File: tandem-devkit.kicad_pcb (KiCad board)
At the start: 2 copper layers, 95.4 x 100 mm, 88 parts, among them J101 Conn_01x02, J102 QWIIC I2C Connector, J301 ConnectorLCDFrontLight, J302 FPC24(0.5MM), J303 FPC10(0.5MM), Q301 2N7002, Q302 2N7002, Q303 AO3401A, U201 AMS1117-ADJ_SOT223

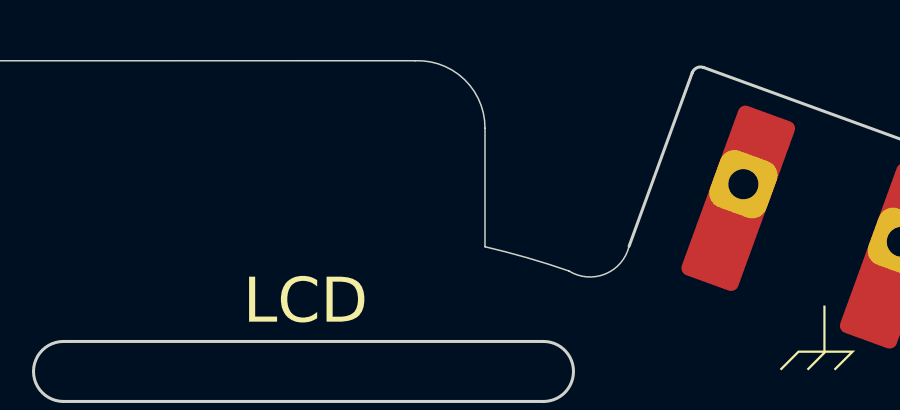
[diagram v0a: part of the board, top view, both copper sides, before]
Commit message: PCB: import JLCPCB 4-Layer board settings
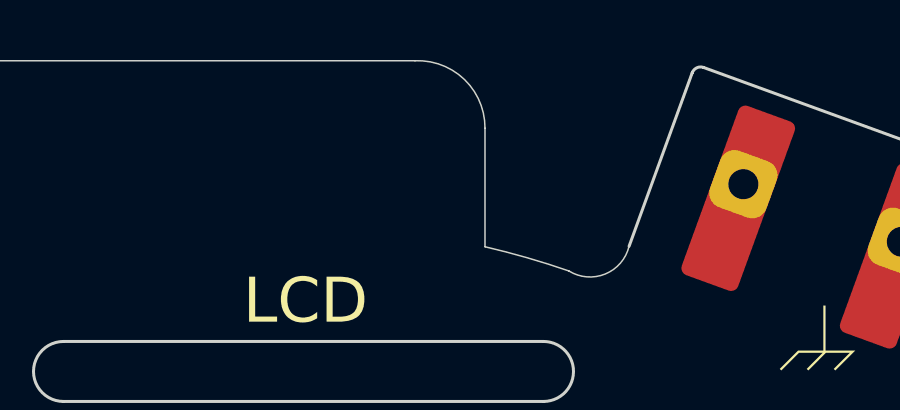
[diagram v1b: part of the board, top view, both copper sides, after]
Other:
- copper layers 2 -> 4
- rule pad_to_mask_clearance: 0.05 -> 0
- rule solder_mask_min_width: 0.2 -> 0.02
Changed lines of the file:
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@@
 (kicad_pcb (version 20211014) (generator pcbnew)
   (general
-    (thickness 1.6)
+    (thickness 4.69)
   )
   (paper "A4")
   (layers
     (0 "F.Cu" signal)
+    (1 "In1.Cu" power)
+    (2 "In2.Cu" power)
     (31 "B.Cu" signal)
-    (32 "B.Adhes" user "B.Adhesive")
-    (33 "F.Adhes" user "F.Adhesive")
     (34 "B.Paste" user)
     (35 "F.Paste" user)
@@
     (38 "B.Mask" user)
     (39 "F.Mask" user)
-    (40 "Dwgs.User" user "User.Drawings")
-    (41 "Cmts.User" user "User.Comments")
-    (42 "Eco1.User" user "User.Eco1")
-    (43 "Eco2.User" user "User.Eco2")
     (44 "Edge.Cuts" user)
     (45 "Margin" user)
@@
     (48 "B.Fab" user)
     (49 "F.Fab" user)
-    (50 "User.1" user "Housing_Outline")
-    (51 "User.2" user)
-    (52 "User.3" user)
-    (53 "User.4" user)
-    (54 "User.5" user)
-    (55 "User.6" user)
-    (56 "User.7" user)
-    (57 "User.8" user)
-    (58 "User.9" user)
   )
   (setup
@@
       (layer "F.Cu" (type "copper") (thickness 0.035))
       (layer "dielectric 1" (type "core") (thickness 1.51) (material "FR4") (epsilon_r 4.5) (loss_tangent 0.02))
+      (layer "In1.Cu" (type "copper") (thickness 0.035))
+      (layer "dielectric 2" (type "prepreg") (thickness 1.51) (material "FR4") (epsilon_r 4.5) (loss_tangent 0.02))
+      (layer "In2.Cu" (type "copper") (thickness 0.035))
+      (layer "dielectric 3" (type "core") (thickness 1.51) (material "FR4") (epsilon_r 4.5) (loss_tangent 0.02))
       (layer "B.Cu" (type "copper") (thickness 0.035))
-      (layer "B.Mask" (type "Bottom Solder Mask") (thickness 0.01))
+      (layer "B.Mask" (type "Bottom Solder Mask") (color "Red") (thickness 0.01))
       (layer "B.Paste" (type "Bottom Solder Paste"))
       (layer "B.SilkS" (type "Bottom Silk Screen"))
@@
       (dielectric_constraints yes)
     )
-    (pad_to_mask_clearance 0.05)
-    (solder_mask_min_width 0.2)
+    (pad_to_mask_clearance 0)
+    (solder_mask_min_width 0.02)
     (aux_axis_origin 284.994474 12.014472)
     (pcbplotparams
@@
     (fp_arc (start -45.696302 -20.932495) (mid -45.683648 -19.701061) (end -46.40509 -18.703007) (layer "Edge.Cuts") (width 0.05))
     (fp_arc (start 36.906133 -30.598692) (mid 37.06124 -30.768019) (end 37.290647 -30.777994) (layer "Edge.Cuts") (width 0.1))
-    (fp_arc (start 46.190086 -18.7) (mid 47.148177 -17.498337) (end 47.490086 -16) (layer "Edge.Cuts") (width 0.1))
+    (fp_arc (start 46.190086 -18.7) (mid 47.148169 -17.498338) (end 47.490086 -16) (layer "Edge.Cuts") (width 0.1))
     (fp_arc (start 47.490086 66.5) (mid 46.848778 68.178963) (end 45.25 69) (layer "Edge.Cuts") (width 0.05))
     (fp_arc (start -37.542423 -30.767616) (mid -37.30035 -30.764463) (end -37.121137 -30.601698) (layer "Edge.Cuts") (width 0.05))
-    (fp_arc (start 27.666822 -31.00341) (mid 29.316689 -30.377074) (end 30 -28.75) (layer "Edge.Cuts") (width 0.05))
+    (fp_arc (start 27.666822 -31.00341) (mid 29.316654 -30.377068) (end 30 -28.75) (layer "Edge.Cuts") (width 0.05))
     (fp_arc (start 30 -24.803362) (mid 31.407999 -24.436724) (end 32.79491 -23.996993) (layer "Edge.Cuts") (width 0.05))
     (pad "1" thru_hole roundrect locked (at -38.828584 -26.894123 20) (size 2 2) (drill 1) (layers *.Cu *.Mask) (roundrect_rratio 0.25))

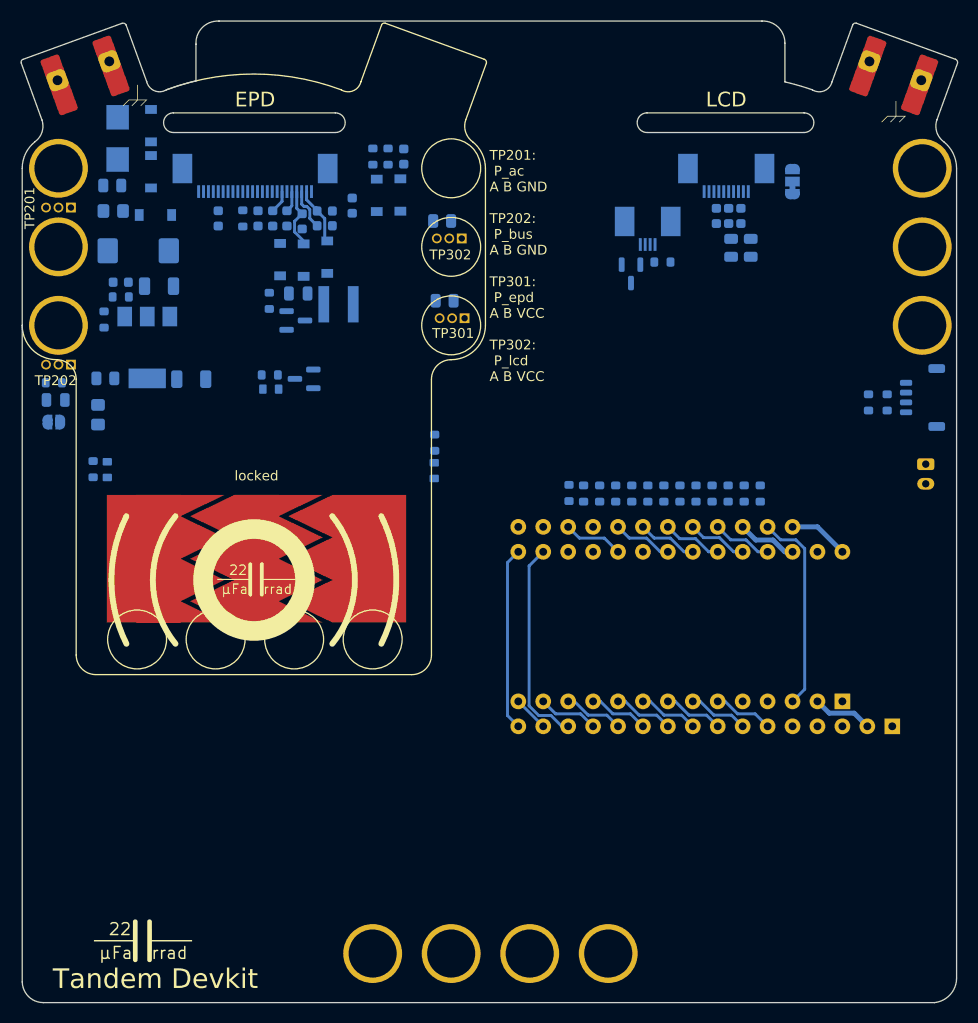
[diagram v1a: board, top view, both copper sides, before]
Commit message: PCB: fix DRC
- reduced track clearance for power and default net to fit between
  the pads of connectors
- rearranged epaper driver to adhere to DRC rules
- connected Feather and ItsyBitsy footprint and the related resistors
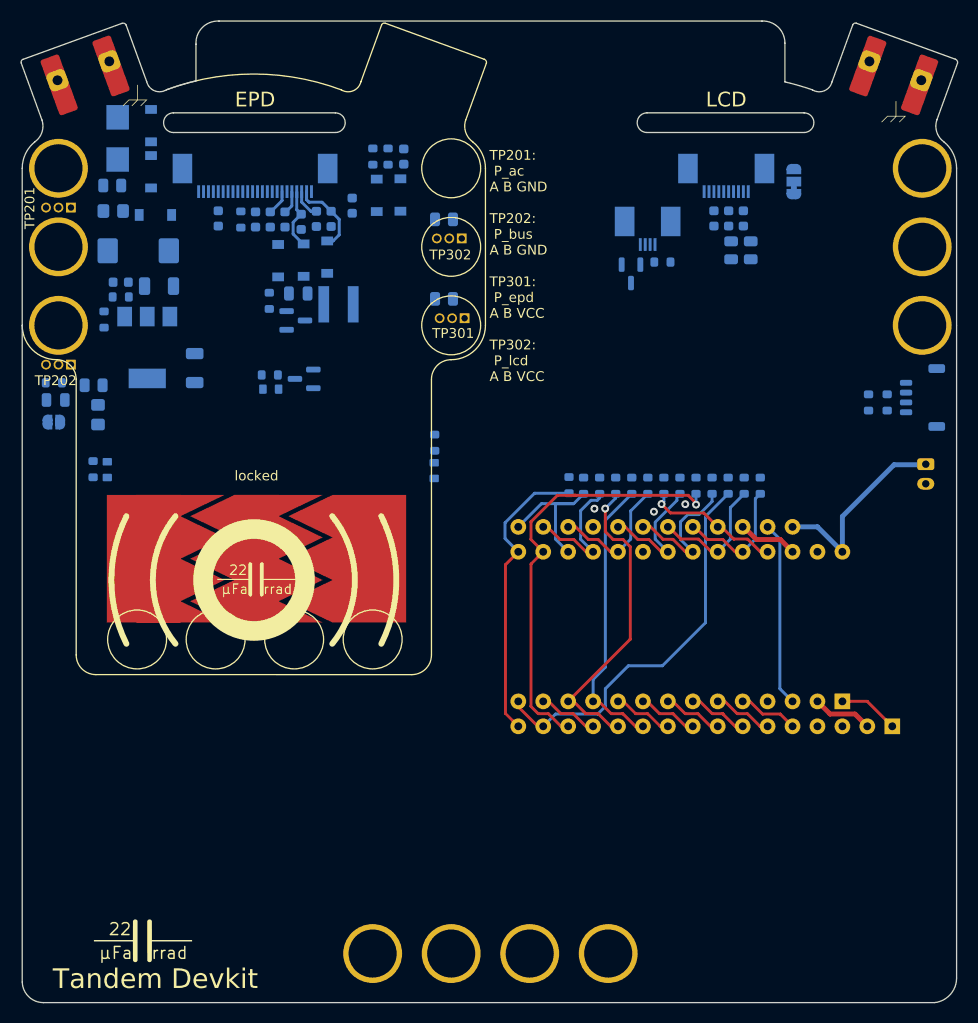
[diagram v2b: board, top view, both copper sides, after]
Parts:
- moved R207 1.39 mm to (127.0, 65.2)
- moved C205 1.18 mm to (137.3, 63.5), turned to 90 degrees
- moved C308 1.10 mm to (149.8, 48.3), turned to 90 degrees
- moved C310 1.03 mm to (151.2, 48.3), turned to 90 degrees
- moved R101 0.80 mm to (175.5, 75.4)
- moved R102 0.80 mm to (183.5, 75.5)
- moved R103 0.80 mm to (186.8, 75.5)
- moved R104 0.80 mm to (190.1, 75.5)
- moved R105 0.80 mm to (193.3, 75.5)
- moved R106 0.80 mm to (195.0, 75.5)
- moved R107 0.80 mm to (185.2, 75.5)
- moved R108 0.80 mm to (181.9, 75.5)
- moved R109 0.80 mm to (180.2, 75.5)
- moved R110 0.80 mm to (188.4, 75.5)
- moved R111 0.80 mm to (191.7, 75.5)
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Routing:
- net Net-(A101-Pad16): track 3.59 -> 40.0 mm
- net Net-(A101-Pad12): track 6.13 -> 32.0 mm, vias 0 -> 1
- net Net-(A101-Pad15): track 21.1 -> 44.2 mm, vias 0 -> 1
- net Net-(A101-Pad11): track 6.13 -> 28.9 mm
- net Net-(A101-Pad17): track 0.00 -> 15.3 mm
- net +BATT: track 6.13 -> 20.4 mm
- net Net-(A101-Pad18): track 0.00 -> 13.7 mm
- net Net-(A101-Pad14): track 18.7 -> 30.1 mm
- net Net-(A101-Pad22): track 6.13 -> 14.6 mm
- net Net-(A101-Pad25): track 6.13 -> 14.0 mm, vias 0 -> 1
- net Net-(A101-Pad21): track 6.13 -> 13.6 mm
- net Net-(A101-Pad19): track 6.13 -> 13.3 mm
- net Net-(A101-Pad23): track 6.13 -> 13.2 mm
- net Net-(A101-Pad24): track 6.13 -> 12.8 mm
- net /CAP_TOUCH_1: track 0.00 -> 6.13 mm
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- added copper zone on In1.Cu, net GND
- added copper zone on In2.Cu, net GND

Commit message: PCB: route display connectors
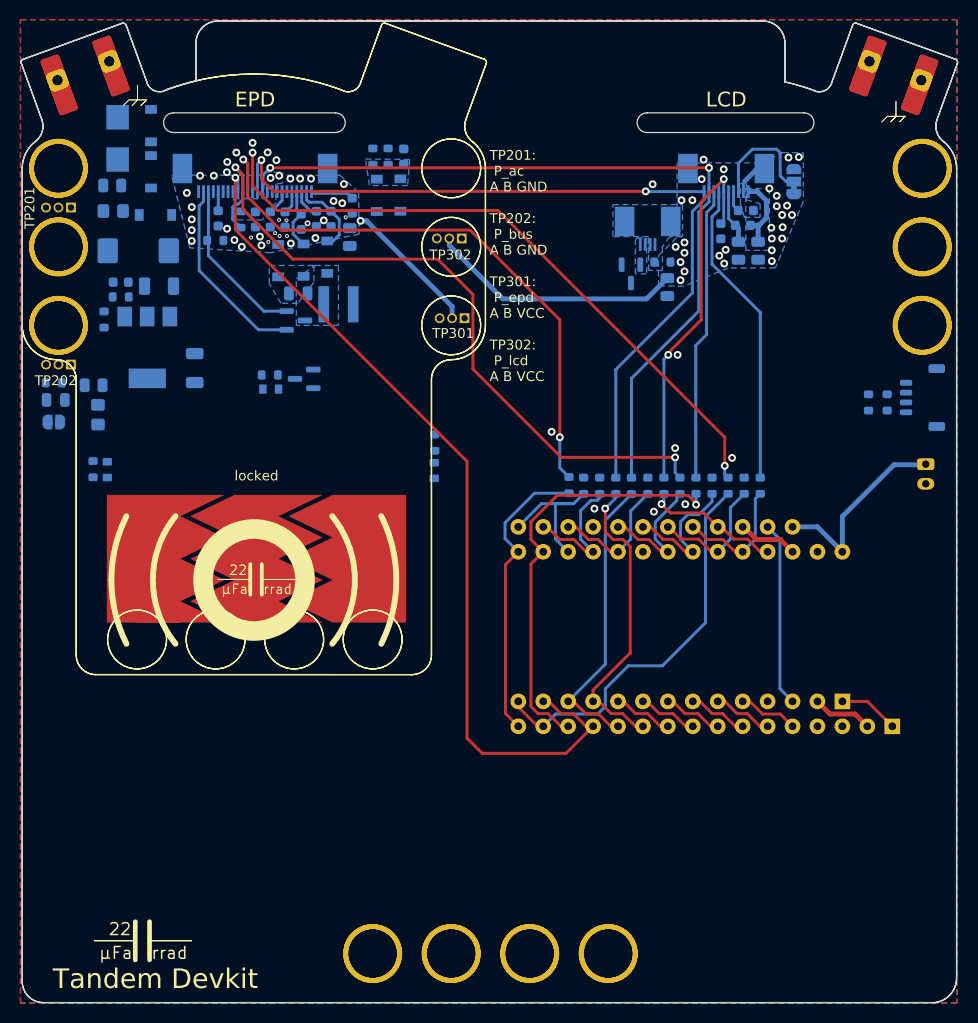
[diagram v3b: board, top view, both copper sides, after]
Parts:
- added REF**: μFahrrad-DevTandem-Shape, project-lib:μFahrrad-DevTandem-Shape, F.Cu at (167.5, 59.1)
- moved R302 23.8 mm to (185.5, 55.2), turned to 90 degrees
- moved R301 11.5 mm to (153.2, 50.1), turned to 90 degrees
- moved R307 8.25 mm to (139.4, 50.5), turned to 0 degrees
- moved R108 1.63 mm to (180.2, 75.5)
- moved C306 1.61 mm to (193.2, 49.0), turned to 0 degrees
- moved R109 1.61 mm to (181.8, 75.5)
- moved C309 1.48 mm to (190.9, 49.5)
- moved C302 0.84 mm to (193.5, 47.5), turned to 0 degrees
- moved FB301 0.75 mm to (192.8, 51.5)
- moved FB302 0.75 mm to (194.8, 51.5)
- turned R308 to -90 degrees
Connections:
- C306 pad 2: /LCD_CURRENT_SENSE -> /Display/GNDA_LCD
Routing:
- net /SPI_SCK: track 0.00 -> 83.8 mm, vias 0 -> 2
- net /~{EPD_BUSY}: track 6.13 -> 89.1 mm, vias 0 -> 1
- net /SPI_MOSI: track 0.00 -> 82.3 mm, vias 0 -> 2
- net /~{EPD_RESET}: track 0.00 -> 73.2 mm, vias 0 -> 2
- net /EPD_SPI_CS: track 0.00 -> 70.3 mm, vias 0 -> 2
- net /EPD_D/C: track 0.00 -> 60.8 mm, vias 0 -> 2
- net /LCD_DISP: track 0.00 -> 37.6 mm, vias 0 -> 2
- net /LCD_EXTCOM: track 0.00 -> 31.5 mm
- net /LCD_SPI_CS: track 0.00 -> 29.9 mm
- net /LCD_CURRENT_SENSE: track 6.13 -> 35.8 mm, vias 0 -> 26
- net /Display/GDR: track 0.00 -> 19.6 mm
- net /Display/RESE: track 0.00 -> 16.8 mm
- net /EPD_CURRENT_SENSE: track 6.13 -> 20.3 mm, vias 0 -> 31
- net /Display/EXTMODE: track 0.00 -> 11.9 mm
- net /Display/GNDA_LCD: track 0.00 -> 7.55 mm
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- added copper zone on B.Cu, net /Display/CP_INT1
- added copper zone on B.Cu, net /Display/CP_INT2
- added copper zone on B.Cu, net /Display/GNDA_LCD
- added copper zone on B.Cu, net /EPD_CURRENT_SENSE
- added copper zone on In2.Cu, net /EPD_CURRENT_SENSE
- added copper zone on B.Cu, net /LCD_CURRENT_SENSE
- added copper zone on In2.Cu, net /LCD_CURRENT_SENSE
- added copper zone on B.Cu, net /SIG_RPM
- added copper zone on B.Cu, net GND
- added copper zone on F.Cu, net GND
- added copper zone on B.Cu, net Net-(J301-Pad1)
- added copper zone on B.Cu, net Net-(J301-Pad3)
- added copper zone on B.Cu, net VCC

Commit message: PCB: routing mostly done
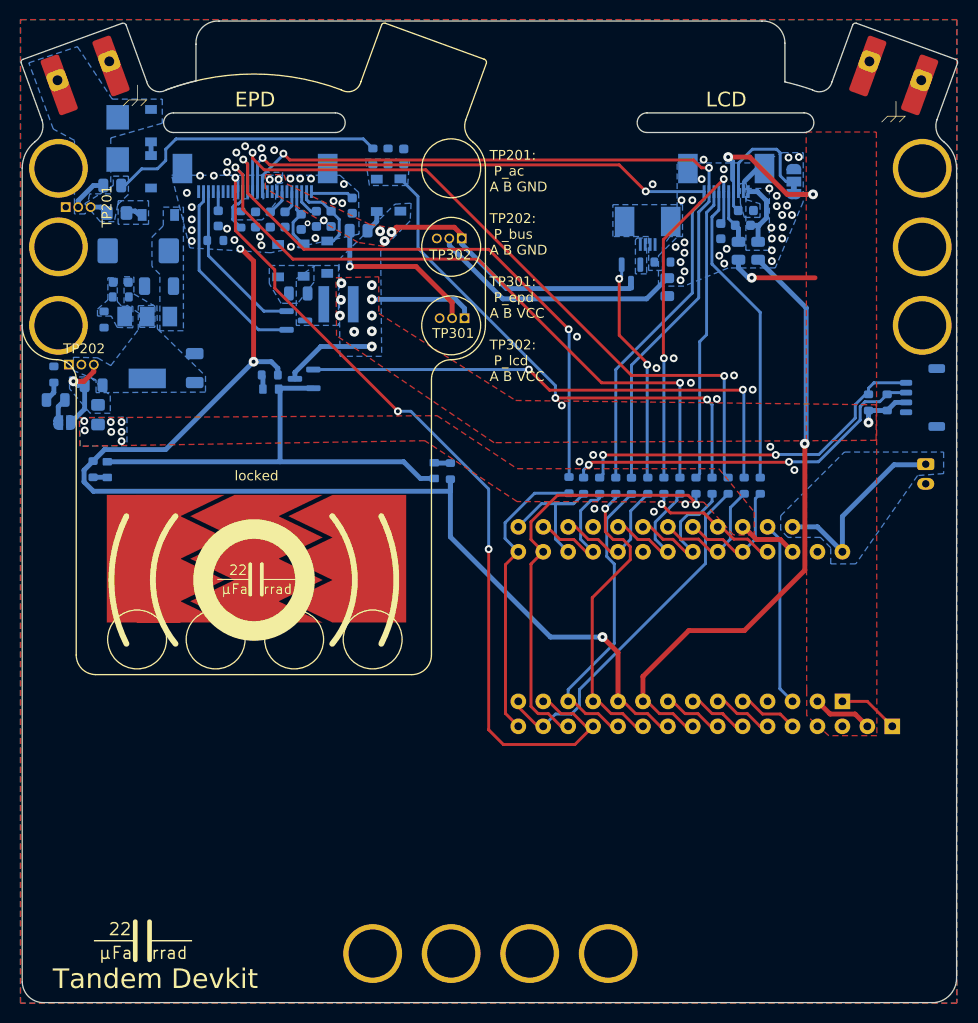
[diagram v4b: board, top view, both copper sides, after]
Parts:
- removed the REF** at (167.5, 59.1) (x2)
- added REF**: μFahrrad-DevTandem-Shape, project-lib:μFahrrad-DevTandem-Shape, F.Cu at (167.5, 59.1)
- moved R306 3.31 mm to (163.4, 74.0), turned to -90 degrees
- moved R301 1.11 mm to (154.1, 49.5), turned to 180 degrees
- moved JP201 1.10 mm to (124.1, 69.0)
- moved R208 0.85 mm to (123.0, 64.2), turned to 90 degrees
- moved TP201 0.53 mm to (124.2, 47.1), turned to -90 degrees
- moved R202 0.40 mm to (129.4, 47.7)
- moved D204 0.30 mm to (133.7, 47.9)
- moved TP202 0.21 mm to (124.5, 63.1), turned to -90 degrees
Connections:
- A101 pad 10: /LCD_CURRENT_SENSE -> /EPD_CURRENT_SENSE
- A101 pad 9: /EPD_CURRENT_SENSE -> /LCD_CURRENT_SENSE
- A102 pad 10: /LCD_CURRENT_SENSE -> /EPD_CURRENT_SENSE
- A102 pad 9: /EPD_CURRENT_SENSE -> /LCD_CURRENT_SENSE
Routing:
- net /EPD_CURRENT_SENSE: track 20.3 -> 133.7 mm, vias 31 -> 25
- net VCC: track 8.26 -> 87.3 mm, vias 2 -> 18
- net /LCD_CURRENT_SENSE: track 35.8 -> 93.1 mm, vias 26 -> 27
- net /EPD_BL: track 0.00 -> 53.7 mm, vias 0 -> 2
- net /SIG_RPM: track 0.00 -> 52.6 mm, vias 0 -> 2
- net Net-(D301-Pad2): track 0.00 -> 45.1 mm
- net /I2C_SDA: track 0.00 -> 37.7 mm, vias 0 -> 2
- net /I2C_SCL: track 0.00 -> 37.5 mm, vias 0 -> 2
- net Net-(J203-Pad1): track 0.00 -> 30.6 mm
- net /LCD_BL: track 0.00 -> 23.0 mm, vias 0 -> 2
- net Net-(JP201-Pad1): track 0.00 -> 8.87 mm, vias 0 -> 1
- net /power-A/V_DYNAMO_AC: track 0.00 -> 3.90 mm
- net Net-(A101-Pad16): track 40.0 -> 36.4 mm
- net Net-(D207-Pad2): track 0.00 -> 2.58 mm
- net GND: track 0.00 -> 2.34 mm, vias 16 -> 24
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- added copper zone on B.Cu, net +BATT
- added copper zone on B.Cu, net /power-A/FB
- added copper zone on B.Cu, net /power-A/V_DYNAMO_AC
- added copper zone on B.Cu, net /power-A/V_RECT
- added copper zone on B.Cu, net Net-(C204-Pad1)
- added copper zone on B.Cu, net Net-(D204-Pad2)
- added copper zone on B.Cu, net Net-(J203-Pad1)
- added copper zone on B.Cu, net Net-(JP201-Pad1)
- added copper zone on B.Cu, net VBUS
- added copper zone on F.Cu, net VBUS
- added copper zone on F.Cu, net VCC
